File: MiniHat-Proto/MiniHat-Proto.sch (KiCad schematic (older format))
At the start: 1 part, among them J101 Interface

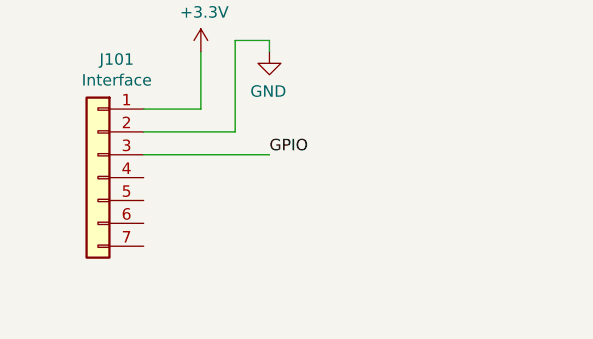
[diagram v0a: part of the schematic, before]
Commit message: New GND Pin.  Added PI Filters to all inputs.    Refined Layout
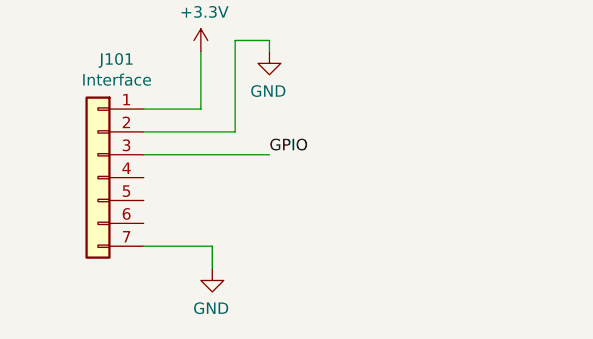
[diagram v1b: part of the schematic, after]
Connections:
- net GND: now also J101.7 (Pin_7)
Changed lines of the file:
@@
 Wire Wire Line
 	1600 2600 2150 2600
+$Comp
+L power:GND #PWR0101
+U 1 1 5FBFDED8
+P 1900 3100
+AR Path="/5FBFDED8" Ref="#PWR0101"  Part="1"
+AR Path="/5C3476D8/5FBFDED8" Ref="#PWR?"  Part="1"
+AR Path="/5CA65CC5/5FBFDED8" Ref="#PWR?"  Part="1"
+AR Path="/5F6FAF6E/5FBFDED8" Ref="#PWR?"  Part="1"
+AR Path="/5FB0E40B/5FBFDED8" Ref="#PWR?"  Part="1"
+AR Path="/5FB12AF7/5FBFDED8" Ref="#PWR?"  Part="1"
+F 0 "#PWR0101" H 1900 2850 50  0001 C CNN
+F 1 "GND" H 1905 2927 50  0000 C CNN
+F 2 "" H 1900 3100 50  0001 C CNN
+F 3 "" H 1900 3100 50  0001 C CNN
+	1    1900 3100
+	-1   0    0    -1
+$EndComp
+Wire Wire Line
+	1600 3000 1900 3000
+Wire Wire Line
+	1900 3000 1900 3100
 $EndSCHEMATC
